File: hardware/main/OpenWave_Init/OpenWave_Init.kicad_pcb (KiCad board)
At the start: 2 copper layers, 17.8 x 15.2 mm, 2 parts

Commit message: V0.2
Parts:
- removed REF**: MountingHole_3.2mm_M3, MountingHole:MountingHole_3.2mm_M3
- removed REF**: PinHeader_1x02_P2.54mm_Vertical, Connector_PinHeader_2.54mm:PinHeader_1x02_P2.54mm_Vertical
- added BT1: Battery_Cell, Battery:Battery_Panasonic_CR1220-VCN_Vertical_CircularHoles, F.Cu at (227.8, 85.4)
- added C1: 1uF, PCM_JLCPCB:C_0402, F.Cu at (217.3, 92.0)
- added C10: 2.2uF, PCM_JLCPCB:C_0603, F.Cu at (226.5, 112.2)
- added C11: 100nF, PCM_JLCPCB:C_0402, F.Cu at (235.8, 100.2)
- added C12: 10uF, PCM_JLCPCB:C_0603, F.Cu at (225.0, 75.7)
- added C13: 10uF, PCM_JLCPCB:C_0603, F.Cu at (233.5, 75.7)
- added C14: 10uF, PCM_JLCPCB:C_0603, F.Cu at (213.4, 78.1)
- added C15: 100nF, PCM_JLCPCB:C_0402, F.Cu at (214.7, 77.8)
- added C16: 1uF, PCM_JLCPCB:C_0402, F.Cu at (178.2, 90.6)
- added C17: 22uF, PCM_JLCPCB:C_0805, F.Cu at (220.9, 77.8)
- added C18: 22uF, PCM_JLCPCB:C_0805, F.Cu at (222.9, 77.8)
- added C19: 1uF, PCM_JLCPCB:C_0402, F.Cu at (172.5, 92.8)
- added C2: 100nF, PCM_JLCPCB:C_0402, F.Cu at (217.2, 91.0)
- added C20: 10uF, PCM_JLCPCB:C_0603, F.Cu at (172.0, 94.6)
- added C21: 22uF, PCM_JLCPCB:C_0805, F.Cu at (170.7, 99.1)
- added C22: 4.7uF, PCM_JLCPCB:C_0603, F.Cu at (187.3, 97.9)
- added C23: 4.7uF, PCM_JLCPCB:C_0603, F.Cu at (187.3, 92.9)
- added C24: 100pF, PCM_JLCPCB:C_0402, F.Cu at (243.7, 115.5)
- added C25: 100pF, PCM_JLCPCB:C_0402, F.Cu at (243.7, 113.5)
- added C26: 100pF, PCM_JLCPCB:C_0402, F.Cu at (244.7, 111.6)
- added C27: 100nF, PCM_JLCPCB:C_0402, F.Cu at (184.5, 101.2)
- added C28: 1uF, PCM_JLCPCB:C_0402, F.Cu at (187.5, 99.2)
- added C29: 100nF, PCM_JLCPCB:C_0402, F.Cu at (190.2, 99.8)
- added C3: 100nF, PCM_JLCPCB:C_0402, F.Cu at (211.5, 95.2)
- added C30: 100nF, PCM_JLCPCB:C_0402, F.Cu at (183.2, 103.5)
- added C31: 100nF, PCM_JLCPCB:C_0402, F.Cu at (193.5, 103.5)
- added C32: 10nF, PCM_JLCPCB:C_0402, F.Cu at (154.5, 105.0)
- added C33: 10nF, PCM_JLCPCB:C_0402, F.Cu at (147.0, 105.5)
- added C34: 10uF, PCM_JLCPCB:C_CASE-A-3216-18(mm), F.Cu at (180.0, 89.3)
- added C35: 10uF, PCM_JLCPCB:C_0603, F.Cu at (219.2, 70.7)
- added C36: 2.2uF, PCM_JLCPCB:C_0603, F.Cu at (210.2, 106.5)
- added C37: 100nF, PCM_JLCPCB:C_0402, F.Cu at (222.8, 91.7)
- added C38: 100nF, PCM_JLCPCB:C_0402, F.Cu at (225.0, 91.9)
- added C39: 10uF, PCM_JLCPCB:C_0603, F.Cu at (213.1, 110.4)
- added C4: 100nF, PCM_JLCPCB:C_0402, F.Cu at (211.5, 107.2)
- added C40: 220nF, PCM_JLCPCB:C_0402, F.Cu at (179.0, 114.5)
- added C41: 1.5nF, PCM_JLCPCB:C_0603, F.Cu at (179.2, 103.2)
- added C42: 100pF, PCM_JLCPCB:C_0402, F.Cu at (178.0, 106.5)
- added C43: 680pF, PCM_JLCPCB:C_0402, F.Cu at (182.0, 105.2)
- added C44: 680pF, PCM_JLCPCB:C_0402, F.Cu at (189.5, 105.8)
- added C45: 1.5nF, PCM_JLCPCB:C_0603, F.Cu at (189.5, 102.5)
- added C46: 100pF, PCM_JLCPCB:C_0402, F.Cu at (192.0, 107.5)
- added C47: 220nF, PCM_JLCPCB:C_0402, F.Cu at (193.0, 114.3)
- added C48: 100nF, PCM_JLCPCB:C_0402, F.Cu at (269.2, 67.0)
- added C49: 6.8pF, PCM_JLCPCB:C_0402, F.Cu at (269.2, 68.8)
- added C5: 100nF, PCM_JLCPCB:C_0402, F.Cu at (227.0, 111.0)
- added C50: 6.8pF, PCM_JLCPCB:C_0402, F.Cu at (269.2, 70.7)
- added C51: 10nF, PCM_JLCPCB:C_0402, F.Cu at (269.2, 72.5)
- added C52: 15pF, PCM_JLCPCB:C_0402, F.Cu at (269.2, 74.4)
- added C53: 15pF, PCM_JLCPCB:C_0402, F.Cu at (269.2, 76.2)
- added C54: 10uF, PCM_JLCPCB:C_0603, F.Cu at (269.7, 80.1)
- added C55: 100nF, PCM_JLCPCB:C_0402, F.Cu at (269.2, 78.1)
- added C56: 100nF, PCM_JLCPCB:C_0402, F.Cu at (272.1, 67.0)
- added C57: 100nF, PCM_JLCPCB:C_0402, F.Cu at (272.1, 68.8)
- added C58: 100nF, PCM_JLCPCB:C_0402, F.Cu at (272.1, 70.7)
- added C59: 100nF, PCM_JLCPCB:C_0402, F.Cu at (272.1, 72.5)
- added C6: 100nF, PCM_JLCPCB:C_0402, F.Cu at (230.7, 95.5)
- added C60: 100nF, PCM_JLCPCB:C_0402, F.Cu at (272.1, 74.4)
- added C61: 100nF, PCM_JLCPCB:C_0402, F.Cu at (272.1, 76.2)
- added C62: 10uF, PCM_JLCPCB:C_0603, F.Cu at (269.7, 82.4)
- added C63: 10nF, PCM_JLCPCB:C_0402, F.Cu at (272.1, 78.1)
- added C64: 4.7uF, PCM_JLCPCB:C_0603, F.Cu at (269.7, 84.6)
- added C7: 10uF, PCM_JLCPCB:C_CASE-A-3216-18(mm), F.Cu at (280.9, 108.4)
- added C8: 10pF, PCM_JLCPCB:C_0402, F.Cu at (220.6, 86.7)
- added C9: 10pF, PCM_JLCPCB:C_0402, F.Cu at (220.6, 91.0)
- added D1: LED, LED_SMD:LED_0603_1608Metric, F.Cu at (160.8, 117.0)
- added D2: SMAJ10CA, PCM_JLCPCB:D_SMA, F.Cu at (222.5, 64.5)
- added D3: TPRCLAMP2451ZA, PCM_JLCPCB:D_DFN0603-2, F.Cu at (233.8, 103.2)
- added D4: TPRCLAMP2451ZA, PCM_JLCPCB:D_DFN0603-2, F.Cu at (236.0, 104.5)
- added D5: TPRCLAMP2451ZA, PCM_JLCPCB:D_DFN0603-2, F.Cu at (237.5, 104.5)
- added D6: TPRCLAMP2451ZA, PCM_JLCPCB:D_DFN0603-2, F.Cu at (236.0, 99.5)
- added D7: TPRCLAMP2451ZA, PCM_JLCPCB:D_DFN0603-2, F.Cu at (237.5, 100.2)
- added FB1: ~, PCM_JLCPCB:FB_0603, F.Cu at (216.8, 88.7)
- added FB2: ~, PCM_JLCPCB:FB_0603, F.Cu at (174.2, 93.6)
- added FB3: ~, PCM_JLCPCB:FB_0603, F.Cu at (187.8, 104.4)
- added FB4: ~, PCM_JLCPCB:FB_0603, F.Cu at (179.8, 100.0)
- added FB5: ~, PCM_JLCPCB:FB_0603, F.Cu at (194.0, 104.8)
- added FB6: ~, PCM_JLCPCB:FB_0805, F.Cu at (216.0, 70.7)
- added FB7: ~, PCM_JLCPCB:FB_0603, F.Cu at (279.0, 81.0)
- added FL1: ACT1210D-101-2P-TL00, A Lot of Stuff:ACT1210D1012PTL00, F.Cu at (240.0, 114.5)
- added FL2: Choke_Coilcraft_0603USB-222, Inductor_SMD:L_CommonModeChoke_Coilcraft_0603USB, F.Cu at (219.4, 115.2)
- added G***: LOGO, A Lot of Stuff:OpenWave_Logo_Silk_50mm, F.Cu at (188.1, 64.8)
- added H1: ~, PCM_JLCPCB:Hole, 3mm, F.Cu at (261.5, 124.0)
- added H2: ~, PCM_JLCPCB:Hole, 3mm, F.Cu at (261.5, 56.0)
- added H3: ~, PCM_JLCPCB:Hole, 3mm, F.Cu at (168.5, 56.0)
- added H4: ~, PCM_JLCPCB:Hole, 3mm, F.Cu at (168.5, 124.0)
- added IC1: TPS7A2050PDBVR, easyeda2kicad:SOT95P280X145-5N, F.Cu at (175.5, 90.1)
- added J1: UART, Connector_PinHeader_2.54mm:PinHeader_1x02_P2.54mm_Vertical, F.Cu at (130.7, 71.5)
- added J2: SWD, Connector_PinHeader_1.00mm:PinHeader_2x03_P1.00mm_Vertical, F.Cu at (237.3, 102.0)
- added J3: FPC 6S, Connector_FFC-FPC:Hirose_FH12-6S-0.5SH_1x06-1MP_P0.50mm_Horizontal, F.Cu at (229.7, 116.5)
- added J4: Barrel_Jack_Switch_MountingPin, A Lot of Stuff:PRT10811, F.Cu at (214.9, 67.0)
- added J5: Control_In, Connector_JST:JST_XH_S2B-XH-A-1_1x02_P2.50mm_Horizontal, F.Cu at (237.7, 121.7)
- added J6: BNC, A Lot of Stuff:5415025-2, F.Cu at (178.5, 120.2)
- added J7: BNC, A Lot of Stuff:5415025-2, F.Cu at (193.5, 120.2)
- added J8: USB_C_Receptacle_USB2.0_16P, Connector_USB:USB_C_Receptacle_GCT_USB4105-xx-A_16P_TopMnt_Horizontal, F.Cu at (219.4, 124.7)
- added J9: RB1-125BAG1A, A Lot of Stuff:RB1125BAG1A, F.Cu at (251.0, 70.5)
- added JP1: SolderJumper, Jumper:SolderJumper-2_P1.3mm_Bridged2Bar_Pad1.0x1.5mm, F.Cu at (225.0, 89.7)
- added JP2: Termination Jumper, Jumper:SolderJumper-2_P1.3mm_Open_Pad1.0x1.5mm, F.Cu at (246.0, 115.9)
- added L1: 22uH, 340mA, Inductor_SMD:L_1210_3225Metric, F.Cu at (174.2, 97.6)
- added PN1: ~, PCM_JLCPCB:Part_Num_JLCPCB, F.Cu at (221.0, 95.7)
- added R1: 10kΩ, PCM_JLCPCB:R_0402, F.Cu at (231.0, 98.2)
- added R10: 4.7kΩ, PCM_JLCPCB:R_0402, F.Cu at (177.2, 87.8)
- added R11: 100kΩ, PCM_JLCPCB:R_0402, F.Cu at (219.4, 75.8)
- added R12: 120Ω, PCM_JLCPCB:R_0402, F.Cu at (246.0, 113.2)
- added R13: 10kΩ, PCM_JLCPCB:R_0402, F.Cu at (184.5, 99.2)
- added R14: 10kΩ, PCM_JLCPCB:R_0402, F.Cu at (190.0, 97.8)
- added R15: 5.1kΩ, PCM_JLCPCB:R_0402, F.Cu at (217.6, 118.5)
- added R16: 5.1kΩ, PCM_JLCPCB:R_0402, F.Cu at (222.1, 118.5)
- added R17: 10kΩ, PCM_JLCPCB:R_0402, F.Cu at (221.1, 118.5)
- added R18: 100Ω, PCM_JLCPCB:R_0603, F.Cu at (179.2, 92.6)
- added R19: 33Ω, PCM_JLCPCB:R_0402, F.Cu at (211.2, 103.5)
- added R2: 1.5kΩ, PCM_JLCPCB:R_0402, F.Cu at (222.9, 111.6)
- added R20: 33Ω, PCM_JLCPCB:R_0402, F.Cu at (211.2, 97.2)
- added R21: 49.9Ω, PCM_JLCPCB:R_0402, F.Cu at (233.7, 101.7)
- added R22: 49.9Ω, PCM_JLCPCB:R_0402, F.Cu at (235.5, 105.5)
- added R23: 49.9Ω, PCM_JLCPCB:R_0402, F.Cu at (237.3, 106.0)
- added R24: 49.9Ω, PCM_JLCPCB:R_0402, F.Cu at (235.8, 98.7)
- added R25: 1Ω, PCM_JLCPCB:R_0402, F.Cu at (179.0, 113.5)
- added R26: 120Ω, PCM_JLCPCB:R_0402, F.Cu at (180.5, 102.8)
- added R27: 1.2kΩ, PCM_JLCPCB:R_0402, F.Cu at (180.5, 104.8)
- added R28: 360Ω, PCM_JLCPCB:R_0603, F.Cu at (179.2, 106.2)
- added R29: 120Ω, PCM_JLCPCB:R_0402, F.Cu at (190.8, 102.8)
- added R3: 3.3kΩ, PCM_JLCPCB:R_0402, F.Cu at (223.0, 110.7)
- added R30: 1.2kΩ, PCM_JLCPCB:R_0402, F.Cu at (190.8, 104.8)
- added R31: 360Ω, PCM_JLCPCB:R_0603, F.Cu at (190.8, 107.2)
- added R32: 1Ω, PCM_JLCPCB:R_0402, F.Cu at (193.0, 113.2)
- added R33: 49.9Ω, PCM_JLCPCB:R_0402, F.Cu at (274.9, 67.0)
- added R34: 49.9Ω, PCM_JLCPCB:R_0402, F.Cu at (274.9, 68.8)
- added R35: 10Ω, PCM_JLCPCB:R_0402, F.Cu at (274.9, 70.7)
- added R36: 220Ω, PCM_JLCPCB:R_0402, F.Cu at (274.9, 72.5)
- added R37: 220Ω, PCM_JLCPCB:R_0402, F.Cu at (274.9, 74.4)
- added R38: 49.9Ω, PCM_JLCPCB:R_0402, F.Cu at (274.9, 76.2)
- added R39: 49.9Ω, PCM_JLCPCB:R_0402, F.Cu at (274.9, 78.1)
- added R4: 330Ω, PCM_JLCPCB:R_0402, F.Cu at (158.0, 117.0)
- added R40: 1MΩ, PCM_JLCPCB:R_0402, F.Cu at (277.8, 67.0)
- added R41: 12kΩ, PCM_JLCPCB:R_0402, F.Cu at (277.8, 68.8)
- added R42: 330Ω, PCM_JLCPCB:R_0402, F.Cu at (277.8, 70.7)
- added R43: 75Ω, PCM_JLCPCB:R_0402, F.Cu at (277.8, 72.5)
- added R5: 4.7kΩ, PCM_JLCPCB:R_0402, F.Cu at (145.5, 84.5)
- added R6: 4.7kΩ, PCM_JLCPCB:R_0402, F.Cu at (154.0, 68.0)
- added R7: 240kΩ, PCM_JLCPCB:R_0603, F.Cu at (217.3, 74.0)
- added R8: 150kΩ, PCM_JLCPCB:R_0402, F.Cu at (217.9, 75.3)
- added R9: 30kΩ, PCM_JLCPCB:R_0603, F.Cu at (215.2, 74.8)
- added U1: STM32H743VITx, Package_QFP:LQFP-100_14x14mm_P0.5mm, F.Cu at (221.0, 101.2)
- added U10: TMP100, Package_TO_SOT_SMD:SOT-23-6, F.Cu at (147.1, 103.2)
- added U11: USBLC6-2P6, Package_TO_SOT_SMD:SOT-666, F.Cu at (219.4, 118.2)
- added U12: W25Q128, PCM_JLCPCB:SOIC-8_L5.3-W5.3-P1.27-LS8.0-BL, F.Cu at (210.3, 114.2)
- added U13: SN74LVC8T245, easyeda2kicad:VQFN-24_L5.6-W3.6-P0.50-BL-EP, F.Cu at (203.0, 89.3)
- added U14: W5500, Package_QFP:LQFP-48_7x7mm_P0.5mm, F.Cu at (285.8, 82.2)
- added U2: AP7363-33D-13, easyeda2kicad:DPAK-3_L6.6-W6.1-P2.28-LS9.9-BR, F.Cu at (229.3, 74.7)
- added U3: TPSM863257RDXR, easyeda2kicad:QFN-7_L4.0-W3.3_TPSM863257RDXR, F.Cu at (217.1, 78.0)
- added U4: REF3333AIDBZR, easyeda2kicad:SOT-23-3_L2.9-W1.6-P1.90-LS2.8-BR, F.Cu at (187.5, 95.4)
- added U5: TJA1051T-3, Package_SO:SOIC-8_3.9x4.9mm_P1.27mm, F.Cu at (242.7, 108.3)
- added U6: LTC2642IMS-16#PBF, easyeda2kicad:MSOP-10_L3.0-W3.0-P0.50-LS4.9-BL, F.Cu at (182.2, 100.0)
- added U7: LMH6658MAX_NOPB, A Lot of Stuff:SOIC127P600X175-8N, F.Cu at (185.2, 108.8)
- added U8: LTC2642IMS-16#PBF, easyeda2kicad:MSOP-10_L3.0-W3.0-P0.50-LS4.9-BL, F.Cu at (192.5, 100.0)
- added U9: TMP100, Package_TO_SOT_SMD:SOT-23-6, F.Cu at (154.3, 102.9)
- added X1: X322525MOB4SI, PCM_JLCPCB:OSC-SMD_4P-L3.2-W2.5-BL, F.Cu at (220.5, 89.0)
- added X2: X322525MOB4SI, PCM_JLCPCB:OSC-SMD_4P-L3.2-W2.5-BL, F.Cu at (274.2, 81.1)
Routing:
- net GND: track 0.00 -> 58.8 mm, vias 0 -> 459
- net (no net): track 55.6 -> 0.00 mm, vias 31 -> 0
- net +5VA: track 0.00 -> 46.7 mm, vias 0 -> 3
- net +5.5V: track 0.00 -> 38.8 mm, vias 0 -> 6
- net DAC_SPI2_MOSI: track 0.00 -> 30.2 mm
- net DAC_SPI2_CLK: track 0.00 -> 26.5 mm
- net +3.3VDAC: track 0.00 -> 26.0 mm
- net DAC_SPI2_CS: track 0.00 -> 24.3 mm
- net /uC_SW_NRST: track 0.00 -> 18.0 mm, vias 0 -> 2
- net +12V: track 0.00 -> 16.6 mm
- net CAN_H: track 0.00 -> 16.5 mm
- net /uC_SW_DIO: track 0.00 -> 16.2 mm, vias 0 -> 2
- net +3V3: track 0.00 -> 15.6 mm, vias 0 -> 1
- net DAC_SPI_MOSI: track 0.00 -> 15.5 mm
- net Wave_OUTB: track 0.00 -> 14.4 mm
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- added copper zone on F.Cu, net +3.3VDAC
- added copper zone on F.Cu, net +5.5V
- added copper zone on F.Cu, net +5VA
- added copper zone on B.Cu, net GND
- added copper zone on F.Cu, net GND
- added copper zone on In1.Cu, net GND
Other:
- board size 17.8 x 15.2 mm -> 100 x 75 mm
- copper layers 2 -> 4

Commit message: WA5500 implementation
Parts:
- removed C60, C61: 100nF, PCM_JLCPCB:C_0402
- moved R40 42.0 mm to (248.2, 96.9)
- moved R36 40.3 mm to (243.3, 97.7), turned to -90 degrees
- moved FB7 38.6 mm to (240.5, 84.0), turned to -90 degrees
- moved U14 38.5 mm to (248.2, 90.7), turned to -90 degrees
- moved R37 38.2 mm to (244.2, 97.2), turned to -90 degrees
- moved R41 38.0 mm to (244.0, 86.2), turned to 180 degrees
- moved R42 37.0 mm to (243.5, 84.7), turned to 90 degrees
- moved C59 36.6 mm to (241.5, 92.7), turned to -90 degrees
- moved R43 35.4 mm to (244.5, 84.7), turned to -90 degrees
- moved C58 35.1 mm to (242.2, 89.2), turned to -90 degrees
- moved C52 34.1 mm to (246.0, 99.4), turned to 90 degrees
- moved C63 33.3 mm to (242.5, 93.4), turned to -90 degrees
- moved R39 33.2 mm to (241.8, 78.5), turned to 180 degrees
- moved X2 31.9 mm to (248.0, 99.3), turned to 90 degrees
- moved R38 31.0 mm to (244.0, 78.4)
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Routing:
- net Net-(J9-K_GREEN): track 0.00 -> 49.1 mm, vias 0 -> 1
- net Net-(J9-K_YELLOW): track 0.00 -> 43.5 mm, vias 0 -> 1
- net /uc_QSPI_IO2: track 2.71 -> 35.0 mm, vias 1 -> 2
- net /uc_QSPI_CLK: track 1.40 -> 20.9 mm, vias 1 -> 2
- net Net-(J9-TD+): track 0.00 -> 17.0 mm, vias 0 -> 2
- net /uc_QSPI_IO1: track 0.00 -> 15.3 mm, vias 0 -> 2
- net Net-(J9-TD-): track 0.00 -> 15.1 mm
- net /uc_QSPI_CS: track 0.00 -> 13.0 mm
- net Net-(U14-RXN): track 0.00 -> 12.5 mm
- net Net-(U14-RXP): track 0.00 -> 11.1 mm, vias 0 -> 2
- net /uc_QSPI_IO0: track 0.00 -> 9.74 mm, vias 0 -> 2
- net /uc_QSPI_IO3: track 0.00 -> 8.95 mm
- net Net-(U14-XO): track 0.00 -> 8.68 mm
- net Net-(C56-Pad1): track 0.00 -> 8.57 mm
- net +5V_USB: track 10.7 -> 18.8 mm, vias 2 -> 3
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
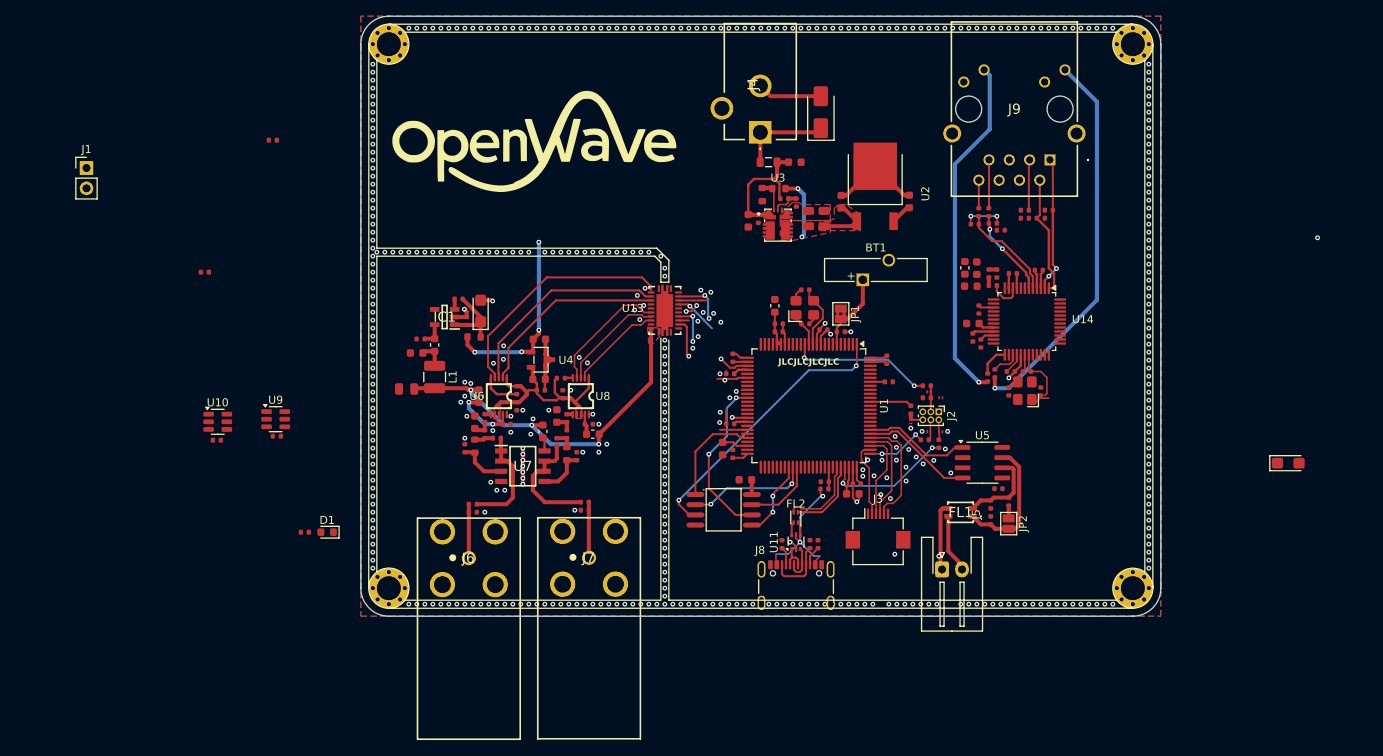
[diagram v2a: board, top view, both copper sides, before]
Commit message: fixed ethernet, impedance, new swiftcircuit logo, arranged schematic
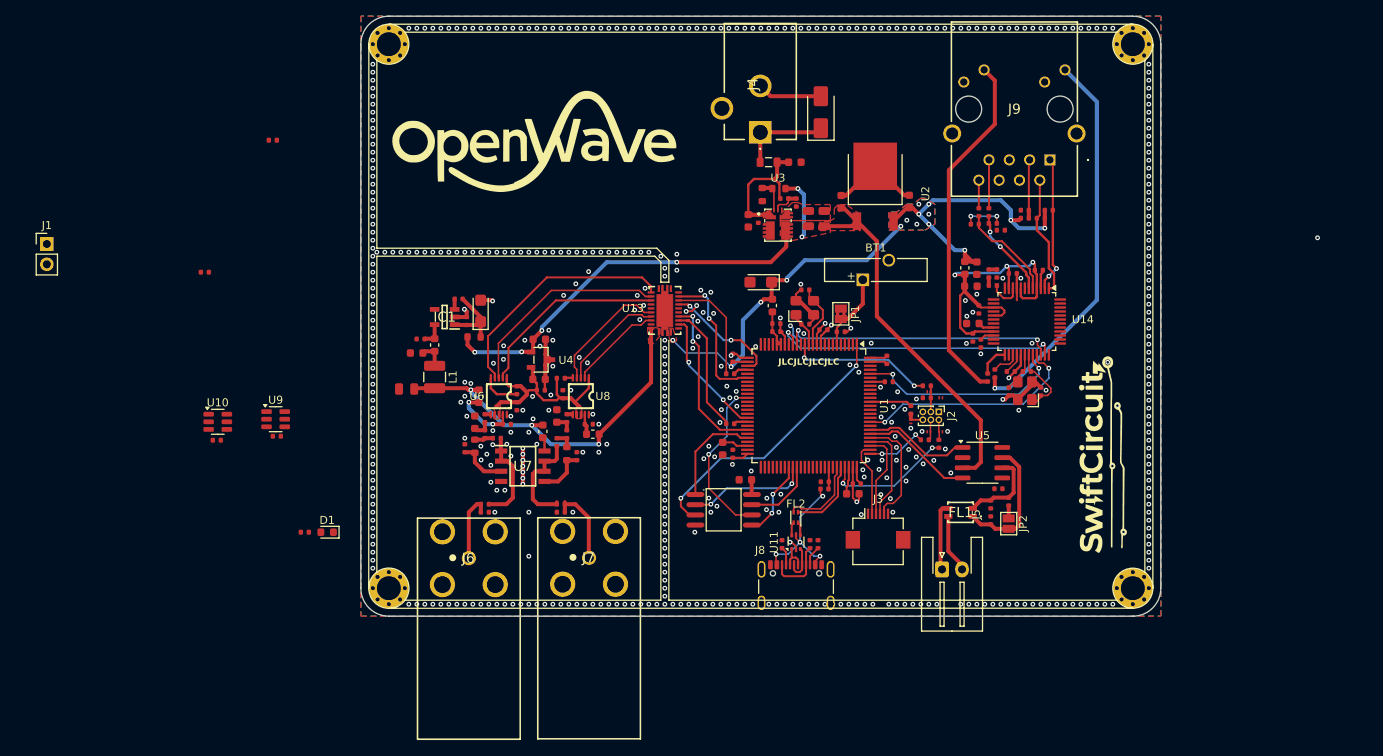
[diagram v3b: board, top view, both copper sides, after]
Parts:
- added G***: LOGO, A Lot of Stuff:SwiftCircuitLogo_Silk_25mm, F.Cu at (257.5, 107.2)
- moved C7 69.7 mm to (215.0, 85.8), turned to 180 degrees
- moved J1 10.7 mm to (125.8, 81.0)
- moved C47 3.01 mm to (190.0, 114.5)
- moved R32 3.01 mm to (190.0, 113.5)
- moved C40 1.50 mm to (180.5, 114.5)
- moved R25 1.50 mm to (180.5, 113.5)
- moved C1 0.31 mm to (216.9, 91.9)
- moved C2 0.31 mm to (216.9, 90.9)
- moved FB1 0.31 mm to (216.4, 88.7)
- turned C9 to 0 degrees
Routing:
- net +3V3: track 18.2 -> 96.4 mm, vias 1 -> 20
- net +5.5V: track 38.8 -> 104.2 mm
- net W55_SPI2_MOSI: track 0.00 -> 36.3 mm, vias 0 -> 2
- net W55_SPI2_MISO: track 0.00 -> 34.7 mm, vias 0 -> 2
- net Net-(C56-Pad1): track 8.57 -> 41.2 mm, vias 0 -> 3
- net W55_SPI2_SCK: track 0.00 -> 28.5 mm, vias 0 -> 2
- net W55_SPI2_CS: track 0.00 -> 26.3 mm, vias 0 -> 2
- net GND: track 66.3 -> 80.2 mm, vias 460 -> 526
- net uC_SPI_CLK: track 3.06 -> 16.4 mm
- net uC_SPI_MOSI: track 8.56 -> 20.9 mm
- net uC_SPI2_CLK: track 3.97 -> 14.2 mm
- net uC_SPI_CS: track 6.84 -> 16.2 mm
- net uC_SPI2_MOSI: track 10.3 -> 18.1 mm
- net uC_SPI2_CS: track 9.39 -> 14.6 mm
- net Net-(J7-In): track 7.07 -> 9.83 mm
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- added copper zone on B.Cu, net +3V3
- added copper zone on F.Cu, net +3V3
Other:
- board text added: "Impedance spec: JLC04161H-2116"
